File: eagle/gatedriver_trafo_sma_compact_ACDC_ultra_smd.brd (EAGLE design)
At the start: 101.9 x 165.1 mm, 88 parts, among them K1 G5V-2, X4 BU-SMA-V

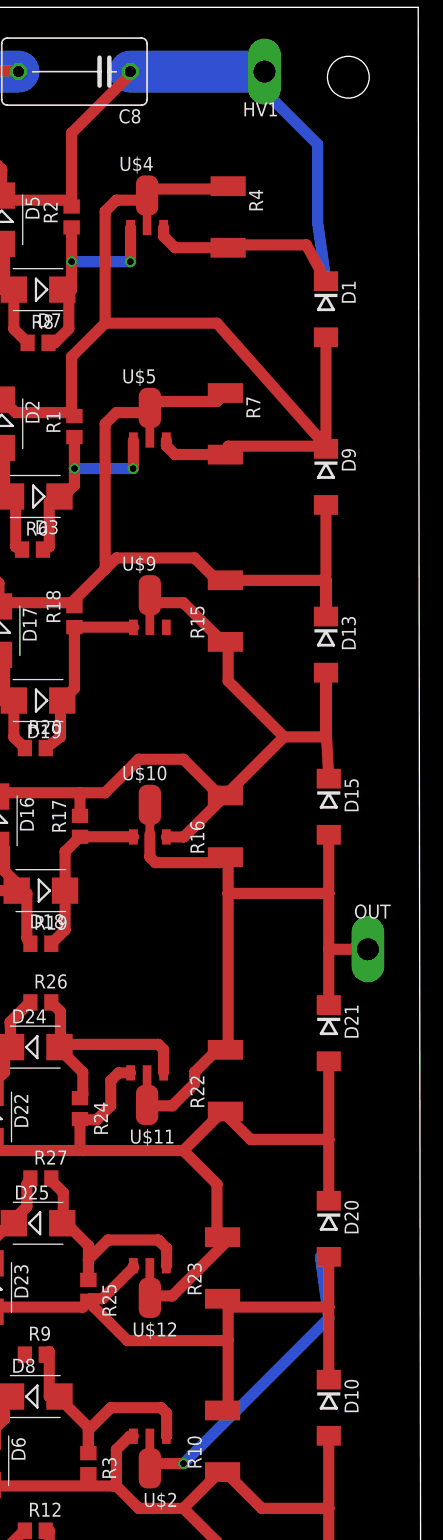
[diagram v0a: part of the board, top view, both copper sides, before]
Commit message: more smd changes
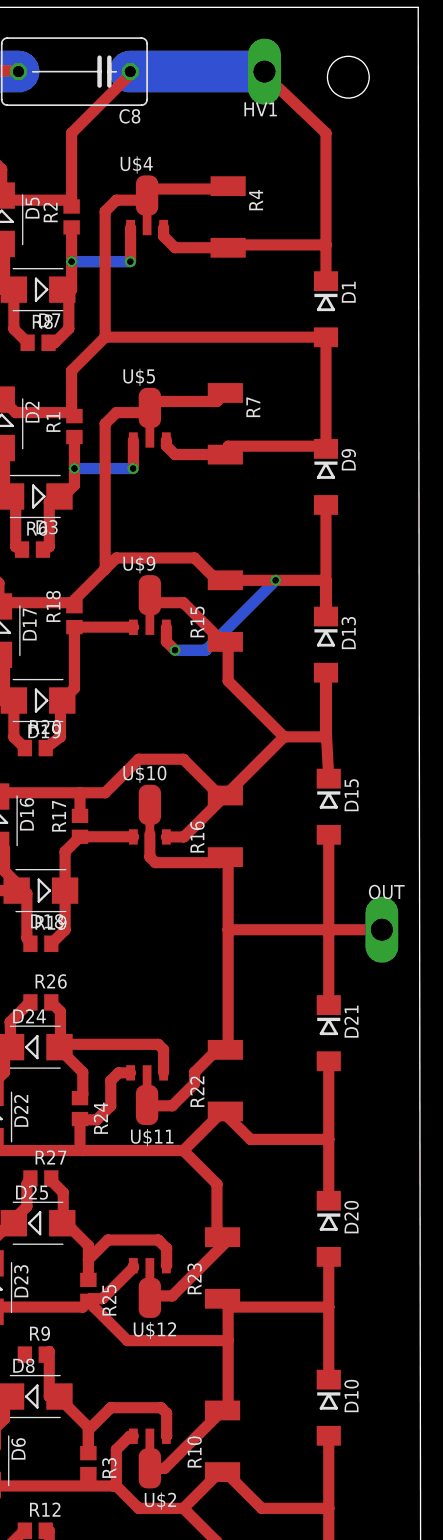
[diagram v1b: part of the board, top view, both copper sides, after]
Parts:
- moved OUT 2.18 mm to (98.3, 81.3)
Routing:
- net N$51: track 110.2 -> 91.2 mm, vias 1 -> 0
- net N$32: track 90.7 -> 104.9 mm, vias 0 -> 2
- net N$18: track 107.3 -> 102.3 mm
- net N$17: track 92.1 -> 90.4 mm
- net N$26: track 65.3 -> 66.6 mm
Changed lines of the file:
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@@
 <element name="D8" library="diode" package="SMB" value="" x="66.802" y="38.862"/>
 <element name="D12" library="diode" package="SMB" value="" x="66.802" y="22.098"/>
-<element name="OUT" library="testpad" package="P1-20Y" value="TPPAD1-20Y" x="97.028" y="79.502">
-<attribute name="TP_SIGNAL_NAME" value="" x="73.406" y="91.186" size="1.778" layer="27" display="off"/>
+<element name="OUT" library="testpad" package="P1-20Y" value="TPPAD1-20Y" x="98.298" y="81.28">
+<attribute name="TP_SIGNAL_NAME" value="" x="74.676" y="92.964" size="1.778" layer="27" display="off"/>
 </element>
 <element name="C10" library="resistor" package="C0805" value=".22u" x="58.166" y="84.836"/>
@@
 <contactref element="R2" pad="2"/>
 <wire x1="75.438" y1="159.258" x2="87.122" y2="159.258" width="3.81" layer="16"/>
-<wire x1="91.44" y1="143.51" x2="84.328" y2="143.51" width="1.016" layer="1"/>
-<wire x1="93.218" y1="140.218" x2="91.44" y2="143.51" width="1.016" layer="1"/>
+<wire x1="93.218" y1="143.51" x2="84.328" y2="143.51" width="1.016" layer="1"/>
 <wire x1="84.328" y1="143.51" x2="84.328" y2="143.25" width="1.016" layer="1"/>
 <wire x1="64.008" y1="147.574" x2="70.104" y2="147.574" width="1.016" layer="1"/>
@@
 <wire x1="87.376" y1="159.766" x2="87.63" y2="159.258" width="1.016" layer="16"/>
 <wire x1="87.376" y1="159.766" x2="87.122" y2="159.258" width="1.016" layer="16"/>
-<wire x1="92.456" y1="152.654" x2="92.456" y2="145.542" width="1.016" layer="16"/>
-<wire x1="87.376" y1="157.734" x2="92.456" y2="152.654" width="1.016" layer="16"/>
-<wire x1="92.456" y1="145.542" x2="93.218" y2="140.218" width="1.016" layer="16"/>
-<wire x1="87.376" y1="157.734" x2="87.63" y2="159.258" width="1.016" layer="16"/>
+<wire x1="93.218" y1="153.67" x2="93.218" y2="143.51" width="1.016" layer="1"/>
+<wire x1="93.218" y1="143.51" x2="93.218" y2="140.218" width="1.016" layer="1"/>
+<wire x1="87.63" y1="159.004" x2="93.218" y2="153.67" width="1.016" layer="1"/>
+<wire x1="87.63" y1="159.004" x2="87.63" y2="159.258" width="1.016" layer="16"/>
 <wire x1="50.4698" y1="147.9677" x2="50.4698" y2="150.7998" width="1.016" layer="1"/>
 <wire x1="50.4698" y1="150.7998" x2="51.308" y2="151.638" width="1.016" layer="1"/>
@@
 <wire x1="78.461" y1="144.297" x2="79.502" y2="143.256" width="1.016" layer="1"/>
 <wire x1="79.502" y1="143.256" x2="83.82" y2="143.256" width="1.016" layer="1"/>
-<wire x1="93.218" y1="140.218" x2="93.218" y2="140.218" width="0" layer="19" extent="1-16"/>
+<wire x1="87.63" y1="159.004" x2="87.63" y2="159.004" width="0" layer="19" extent="1-16"/>
 <wire x1="83.82" y1="143.256" x2="84.328" y2="143.25" width="0" layer="19" extent="1-1"/>
 </signal>
@@
 <wire x1="84.328" y1="148.59" x2="84.328" y2="148.85" width="1.016" layer="1"/>
 <wire x1="77.216" y1="148.59" x2="76.962" y2="148.006" width="1.016" layer="1"/>
-<wire x1="70.104" y1="133.35" x2="70.104" y2="128.27" width="1.016" layer="1"/>
-<wire x1="73.152" y1="136.398" x2="70.104" y2="133.35" width="1.016" layer="1"/>
-<wire x1="73.152" y1="146.558" x2="73.152" y2="136.398" width="1.016" layer="1"/>
+<wire x1="70.104" y1="132.08" x2="70.104" y2="128.27" width="1.016" layer="1"/>
+<wire x1="73.152" y1="135.128" x2="70.104" y2="132.08" width="1.016" layer="1"/>
+<wire x1="73.152" y1="146.558" x2="73.152" y2="135.128" width="1.016" layer="1"/>
 <wire x1="74.168" y1="147.574" x2="73.152" y2="146.558" width="1.016" layer="1"/>
 <wire x1="76.2" y1="147.574" x2="74.168" y2="147.574" width="1.016" layer="1"/>
 <wire x1="70.104" y1="128.27" x2="70.358" y2="127.95" width="1.016" layer="1"/>
 <wire x1="76.2" y1="147.574" x2="76.962" y2="148.006" width="1.016" layer="1"/>
-<wire x1="83.312" y1="136.398" x2="93.218" y2="125.222" width="1.016" layer="1"/>
-<wire x1="73.152" y1="136.398" x2="83.312" y2="136.398" width="1.016" layer="1"/>
+<wire x1="93.218" y1="135.128" x2="93.218" y2="135.118" width="1.016" layer="1"/>
+<wire x1="73.152" y1="135.128" x2="93.218" y2="135.128" width="1.016" layer="1"/>
 <wire x1="52.324" y1="140.5763" x2="52.324" y2="138.938" width="1.016" layer="1"/>
 <via x="52.324" y="138.938" extent="1-16" drill="0.6" shape="square"/>
@@
 <wire x1="84.328" y1="43.942" x2="75.184" y2="43.942" width="1.016" layer="1"/>
 <wire x1="72.136" y1="46.99" x2="71.628" y2="47.564" width="1.016" layer="1"/>
-<wire x1="80.264" y1="32.766" x2="77.216" y2="32.766" width="1.016" layer="1"/>
-<wire x1="93.472" y1="45.974" x2="80.264" y2="32.766" width="1.016" layer="16"/>
-<wire x1="77.216" y1="32.766" x2="77.216" y2="32.334" width="1.016" layer="1"/>
-<wire x1="93.472" y1="45.974" x2="92.71" y2="51.552" width="1.016" layer="16"/>
 <wire x1="93.472" y1="46.99" x2="93.472" y2="40.396" width="1.016" layer="1"/>
 <wire x1="93.472" y1="46.99" x2="84.328" y2="46.99" width="1.016" layer="1"/>
 <wire x1="84.328" y1="46.99" x2="83.82" y2="47.746" width="1.016" layer="1"/>
 <wire x1="93.472" y1="46.99" x2="93.472" y2="51.552" width="1.016" layer="1"/>
-<via x="80.264" y="32.766" extent="1-16" drill="0.6096"/>
 <wire x1="52.9082" y1="62.3443" x2="52.9082" y2="52.2478" width="1.016" layer="1"/>
 <wire x1="52.9082" y1="52.2478" x2="58.674" y2="46.482" width="1.016" layer="1"/>
@@
 <wire x1="72.898" y1="47.752" x2="71.816" y2="47.752" width="1.016" layer="1"/>
 <wire x1="71.816" y1="47.752" x2="71.628" y2="47.564" width="1.016" layer="1"/>
-<wire x1="77.216" y1="32.766" x2="77.216" y2="35.001" width="0" layer="19" extent="1-1"/>
-<wire x1="93.472" y1="51.552" x2="92.71" y2="51.552" width="0" layer="19" extent="1-16"/>
+<wire x1="77.216" y1="32.334" x2="78.556" y2="32.334" width="1.016" layer="1"/>
+<wire x1="78.556" y1="32.334" x2="83.82" y2="37.598" width="1.016" layer="1"/>
+<wire x1="77.216" y1="32.334" x2="77.216" y2="35.001" width="0" layer="19" extent="1-1"/>
 </signal>
 <signal name="N$26">
@@
 <contactref element="U$10" pad="C@1"/>
 <contactref element="U$11" pad="C@1"/>
-<wire x1="93.472" y1="79.502" x2="93.472" y2="84.582" width="1.016" layer="1"/>
-<wire x1="93.472" y1="79.502" x2="97.028" y2="79.502" width="1.016" layer="1"/>
-<wire x1="93.472" y1="79.502" x2="93.472" y2="74.432" width="1.016" layer="1"/>
+<wire x1="93.472" y1="81.28" x2="98.298" y2="81.28" width="1.016" layer="1"/>
+<wire x1="93.472" y1="81.28" x2="93.472" y2="74.432" width="1.016" layer="1"/>
 <wire x1="77.216" y1="92.71" x2="77.216" y2="92.634" width="1.016" layer="1"/>
 <wire x1="81.28" y1="68.326" x2="83.312" y2="70.358" width="1.016" layer="1"/>
@@
 <wire x1="83.312" y1="70.358" x2="84.074" y2="70.364" width="1.016" layer="1"/>
 <wire x1="77.216" y1="65.278" x2="76.962" y2="65.354" width="1.016" layer="1"/>
-<wire x1="84.328" y1="70.358" x2="84.328" y2="84.582" width="1.016" layer="1"/>
-<wire x1="84.328" y1="84.582" x2="84.328" y2="87.63" width="1.016" layer="1"/>
+<wire x1="84.328" y1="70.358" x2="84.328" y2="81.28" width="1.016" layer="1"/>
+<wire x1="84.328" y1="81.28" x2="84.328" y2="87.63" width="1.016" layer="1"/>
 <wire x1="84.328" y1="87.63" x2="84.074" y2="87.878" width="1.016" layer="1"/>
 <wire x1="84.328" y1="70.358" x2="84.074" y2="70.364" width="1.016" layer="1"/>
-<wire x1="84.328" y1="84.582" x2="93.472" y2="84.582" width="1.016" layer="1"/>
-<wire x1="93.472" y1="84.582" x2="93.472" y2="89.906" width="1.016" layer="1"/>
+<wire x1="84.328" y1="81.28" x2="93.472" y2="81.28" width="1.016" layer="1"/>
+<wire x1="93.472" y1="81.28" x2="93.472" y2="89.906" width="1.016" layer="1"/>
 <wire x1="77.216" y1="89.967" x2="77.216" y2="87.884" width="1.016" layer="1"/>
 <wire x1="77.216" y1="87.884" x2="77.724" y2="87.376" width="1.016" layer="1"/>
@@
 <wire x1="64.008" y1="110.998" x2="70.104" y2="110.998" width="1.016" layer="1"/>
 <wire x1="64.008" y1="110.998" x2="63.5" y2="110.658" width="1.016" layer="1"/>
-<wire x1="93.218" y1="113.03" x2="84.328" y2="113.03" width="1.016" layer="1"/>
+<wire x1="93.218" y1="113.03" x2="88.646" y2="113.03" width="1.016" layer="1"/>
+<wire x1="88.646" y1="113.03" x2="84.328" y2="113.03" width="1.016" layer="1"/>
 <wire x1="93.218" y1="109.738" x2="93.218" y2="113.03" width="1.016" layer="1"/>
 <wire x1="84.328" y1="113.03" x2="84.074" y2="113.036" width="1.016" layer="1"/>
@@
 <wire x1="63.5" y1="112.776" x2="63.5" y2="111.506" width="1.016" layer="1"/>
 <wire x1="63.5" y1="111.506" x2="64.008" y2="110.998" width="1.016" layer="1"/>
+<wire x1="78.715" y1="108.763" x2="78.715" y2="107.467" width="1.016" layer="1"/>
+<wire x1="78.715" y1="107.467" x2="79.502" y2="106.68" width="1.016" layer="1"/>
+<via x="79.502" y="106.68" extent="1-16" drill="0.6" shape="square"/>
+<wire x1="79.502" y1="106.68" x2="82.296" y2="106.68" width="1.016" layer="16"/>
+<wire x1="82.296" y1="106.68" x2="88.646" y2="113.03" width="1.016" layer="16"/>
+<via x="88.646" y="113.03" extent="1-16" drill="0.6" shape="square"/>
 <wire x1="77.216" y1="128.27" x2="77.216" y2="126.035" width="0" layer="19" extent="1-1"/>
-<wire x1="78.715" y1="108.763" x2="83.312" y2="113.03" width="0" layer="19" extent="1-1"/>
 </signal>
 </signals>

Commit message: submit smd board
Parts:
- added GND, GND15: TPPAD1-20Y, testpad:P1-20Y
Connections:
- net GND: now also GND.TP, GND15.TP
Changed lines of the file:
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@@
 <element name="D24" library="diode" package="SMB" value="" x="66.802" y="70.612"/>
 <element name="D25" library="diode" package="SMB" value="" x="67.056" y="54.61"/>
+<element name="GND" library="testpad" package="P1-20Y" value="TPPAD1-20Y" x="42.672" y="8.128">
+<attribute name="TP_SIGNAL_NAME" value="" x="42.672" y="8.128" size="1.778" layer="27" display="off"/>
+</element>
+<element name="GND15" library="testpad" package="P1-20Y" value="TPPAD1-20Y" x="42.672" y="159.766">
+<attribute name="TP_SIGNAL_NAME" value="" x="42.672" y="159.766" size="1.778" layer="27" display="off"/>
+</element>
 </elements>
 <signals>
@@
 <wire x1="15.24" y1="74.168" x2="14.478" y2="74.168" width="1.6764" layer="16"/>
 <wire x1="14.478" y1="74.168" x2="13.716" y2="74.168" width="1.6764" layer="16"/>
-<wire x1="46.6852" y1="7.3152" x2="27.180496875" y2="7.34241875" width="3.81" layer="16"/>
-<wire x1="27.180496875" y1="7.34241875" x2="22.606" y2="7.366" width="3.81" layer="16"/>
+<wire x1="46.6852" y1="7.8232" x2="27.180496875" y2="7.85041875" width="3.81" layer="16"/>
+<wire x1="27.180496875" y1="7.85041875" x2="22.606" y2="7.366" width="3.81" layer="16"/>
 <wire x1="14.478" y1="123.444" x2="6.35" y2="123.444" width="1.4224" layer="1"/>
 <via x="6.35" y="123.444" extent="1-16" drill="0.6" shape="square"/>
@@
 <wire x1="64.77" y1="7.874" x2="41.91" y2="7.874" width="3.81" layer="16"/>
 <wire x1="41.91" y1="7.874" x2="27.180496875" y2="7.874" width="3.81" layer="16"/>
-<wire x1="27.180496875" y1="7.874" x2="27.180496875" y2="7.34241875" width="3.81" layer="16"/>
+<wire x1="27.180496875" y1="7.874" x2="27.180496875" y2="7.85041875" width="3.81" layer="16"/>
 <contactref element="U$8" pad="P$2"/>
 <contactref element="U$13" pad="P$2"/>
@@
 <wire x1="51.054" y1="15.24" x2="58.42" y2="7.874" width="1.016" layer="1"/>
 <wire x1="58.42" y1="7.874" x2="64.77" y2="7.874" width="1.016" layer="1"/>
+<contactref element="GND" pad="TP"/>
+<contactref element="GND15" pad="TP"/>
+<wire x1="48.514" y1="152.213175" x2="42.672" y2="159.766" width="0" layer="19" extent="1-1"/>
+<wire x1="42.672" y1="8.128" x2="41.91" y2="7.874" width="0" layer="19" extent="16-16"/>
 </signal>
 <signal name="+15V">

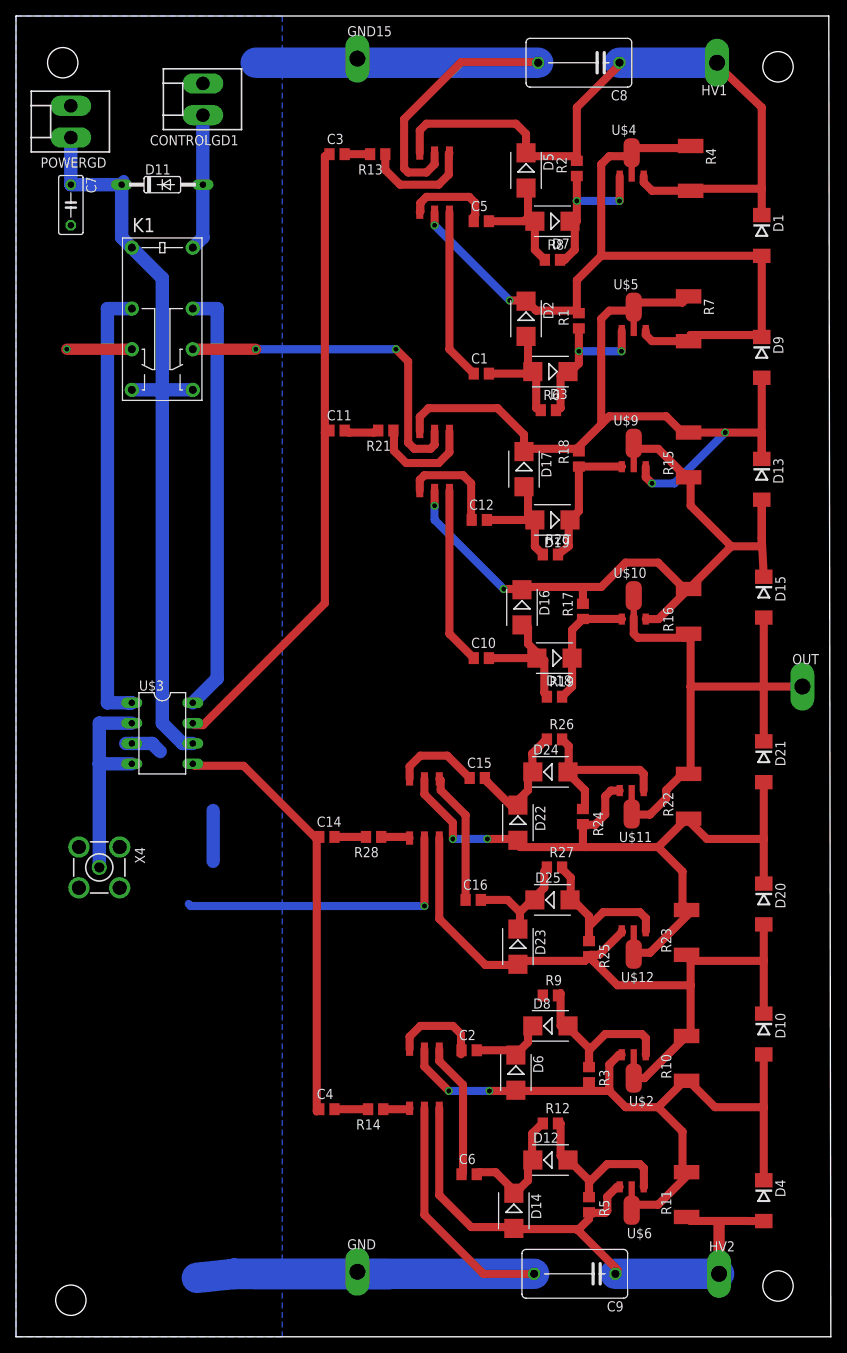
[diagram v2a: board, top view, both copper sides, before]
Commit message: Had the wrong trafo footprint! Fixed now
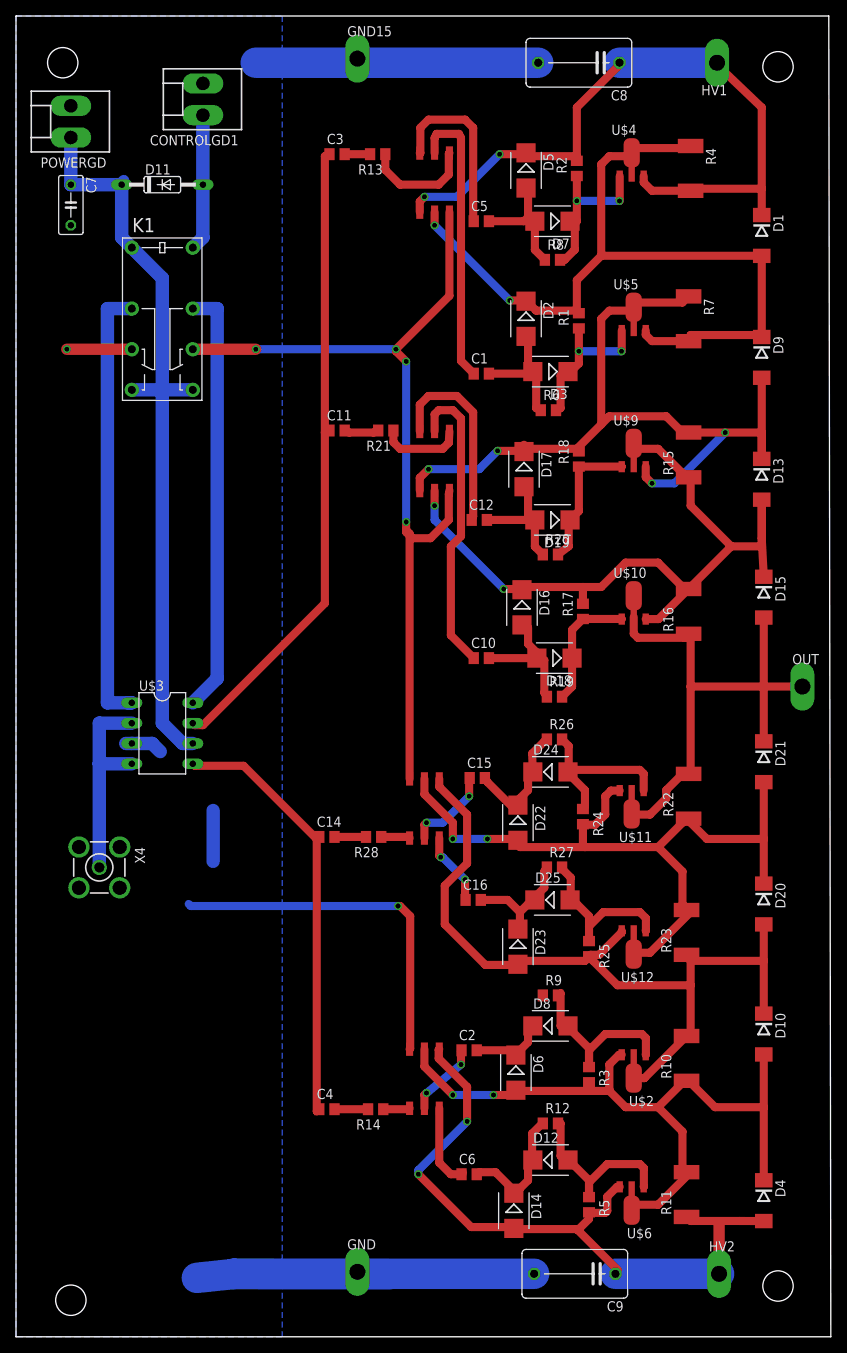
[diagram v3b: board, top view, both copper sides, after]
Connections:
- net GND: now also U$1.P$6, U$13.P$6, U$7.P$6, U$8.P$6; no longer U$1.P$2, U$13.P$2, U$7.P$2, U$8.P$2
- net N$17: now also U$1.P$4; no longer U$1.P$3
- net N$22: now also U$7.P$2; no longer U$7.P$6
- net N$23: now also U$7.P$3; no longer U$7.P$4
- net N$24: now also U$7.P$4; no longer U$7.P$3
- net N$28: now also U$8.P$2; no longer U$8.P$6
- net N$29: now also U$8.P$3; no longer U$8.P$4
- net N$32: now also U$8.P$4; no longer U$8.P$3
- net N$40: now also U$13.P$2; no longer U$13.P$6
- net N$41: now also U$13.P$3; no longer U$13.P$4
- net N$5: now also U$1.P$2; no longer U$1.P$6
- net N$51: now also U$13.P$4; no longer U$13.P$3
- net N$7: now also U$1.P$3; no longer U$1.P$4
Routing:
- net N$28: track 22.2 -> 37.8 mm
- net N$5: track 21.4 -> 35.9 mm
- net N$24: track 76.8 -> 89.3 mm, vias 0 -> 2
- net GND: track 260.8 -> 272.9 mm, vias 4 -> 6
- net N$29: track 13.0 -> 24.8 mm
- net N$7: track 11.0 -> 22.4 mm
- net N$51: track 91.2 -> 100.9 mm
- net N$41: track 16.5 -> 9.25 mm, vias 0 -> 2
- net N$23: track 16.9 -> 10.4 mm
- net N$37: track 13.3 -> 10.5 mm
- net N$17: track 90.4 -> 88.1 mm, vias 0 -> 2
- net N$32: track 104.9 -> 103.0 mm, vias 2 -> 4
- net N$22: track 11.5 -> 10.1 mm, vias 0 -> 2
- net N$13: track 90.5 -> 91.5 mm
- net N$40: track 10.8 -> 11.0 mm, vias 0 -> 2
